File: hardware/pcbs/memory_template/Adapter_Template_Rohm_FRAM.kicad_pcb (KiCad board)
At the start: 2 copper layers, 154.3 x 86.4 mm, 3 parts, among them P1 STM32 Pinheader Left, P2 CONN_02X32_DISCO1_RIGHT_BACK

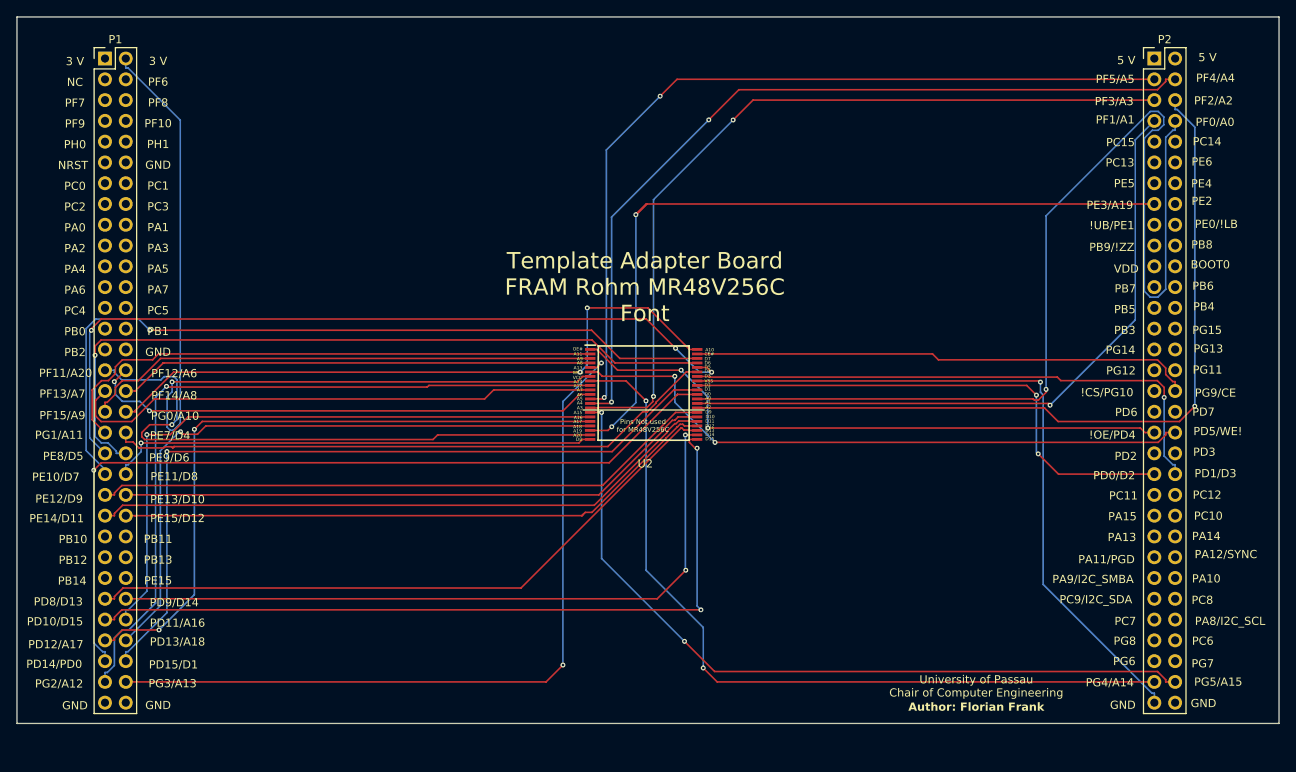
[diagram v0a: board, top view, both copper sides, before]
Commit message: Add README.md and remaining pcb files
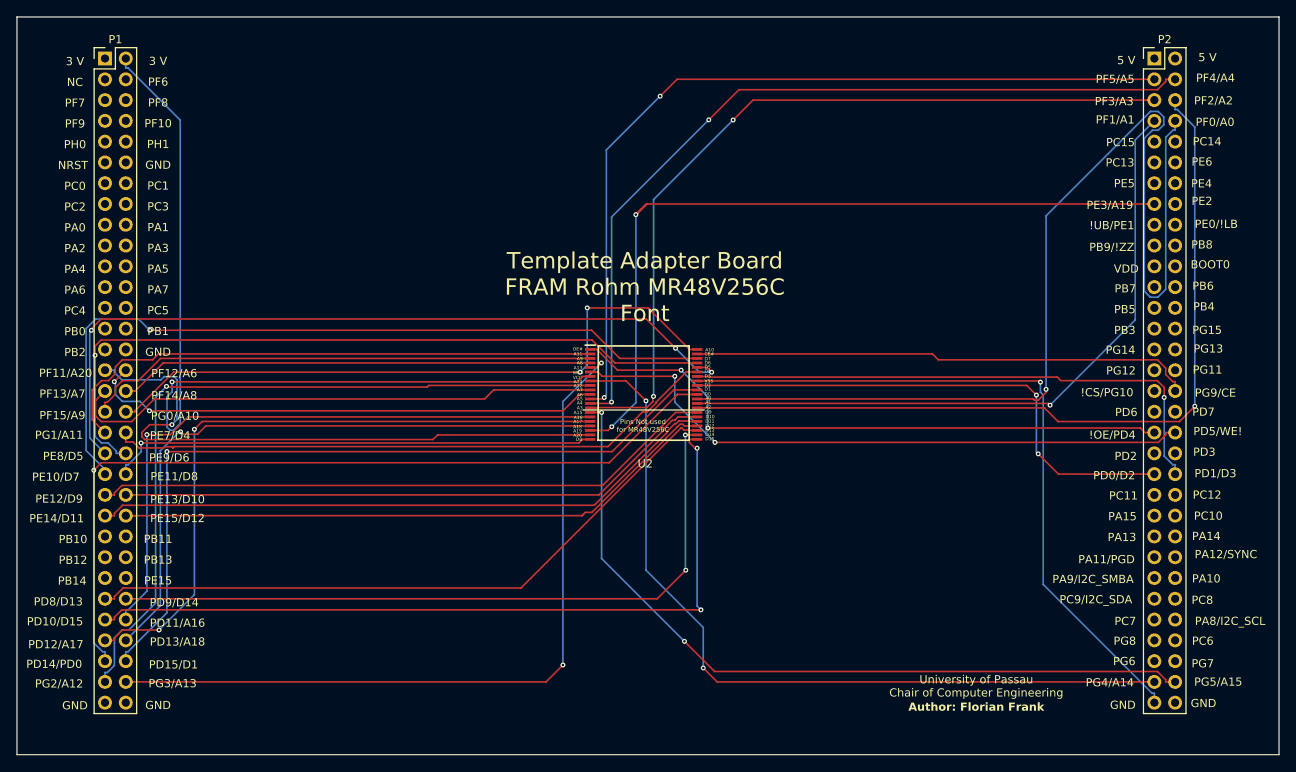
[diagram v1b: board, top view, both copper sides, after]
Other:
- board size 154.3 x 86.4 mm -> 154.3 x 90.2 mm
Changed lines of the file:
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@@
 			(pintype "passive+no_connect")
 		)
-		(model "${KICAD8_3DMODEL_DIR}/Connector_PinHeader_2.54mm.3dshapes/PinHeader_2x32_P2.54mm_Vertical.wrl"
+		(model "${KICAD8_3DMODEL_DIR}/Connector_PinSocket_2.54mm.3dshapes/PinSocket_2x32_P2.54mm_Vertical.wrl"
 			(offset
 				(xyz 0 0 0)
@@
 			)
 			(rotate
-				(xyz 0 0 0)
+				(xyz 0 180 0)
 			)
 		)
@@
 			(pintype "passive+no_connect")
 		)
-		(model "${KICAD8_3DMODEL_DIR}/Connector_PinHeader_2.54mm.3dshapes/PinHeader_2x32_P2.54mm_Vertical.wrl"
+		(model "${KICAD8_3DMODEL_DIR}/Connector_PinSocket_2.54mm.3dshapes/PinSocket_2x32_P2.54mm_Vertical.wrl"
 			(offset
 				(xyz 0 0 0)
@@
 			)
 			(rotate
-				(xyz 0 0 0)
+				(xyz 0 180 0)
 			)
 		)
@@
 	)
 	(gr_line
-		(start 69.25 38.1)
-		(end 69.25 124.46)
+		(start 223.52 38.1)
+		(end 223.52 128.27)
+		(stroke
+			(width 0.15)
+			(type default)
+		)
+		(layer "Edge.Cuts")
+	)
+	(gr_line
+		(start 69.25 128.27)
+		(end 223.52 128.27)
 		(stroke
 			(width 0.05)
@@
 	)
 	(gr_line
-		(start 69.25 124.46)
-		(end 223.52 124.46)
+		(start 69.25 38.1)
+		(end 69.25 128.27)
 		(stroke
-			(width 0.05)
+			(width 0.15)
 			(type default)
 		)
-		(layer "Edge.Cuts")
-	)
-	(gr_line
-		(start 223.52 38.1)
-		(end 223.52 124.46)
-		(stroke
-			(width 0.05)
-			(type default)
-		)
